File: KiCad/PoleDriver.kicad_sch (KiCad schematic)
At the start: 6 parts, among them Q301 AGM6014AP, Q303 AGM6014AP

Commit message: start adding control pins
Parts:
- R301, R302: footprint (none) -> Resistor_SMD:R_0402_1005Metric
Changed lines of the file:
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@@
 					(unit 1)
 				)
-				(path "/0dffc378-5905-459a-b0cb-e8e514a8bbef/e842f42e-62e8-4809-9799-e9078ef99b24/20b87812-a82e-42f6-920a-0aca573365c0"
-					(reference "C801")
-					(unit 1)
-				)
-				(path "/0dffc378-5905-459a-b0cb-e8e514a8bbef/e842f42e-62e8-4809-9799-e9078ef99b24/cd26c950-3a70-43f9-bc93-52ca2ff7311f"
-					(reference "C901")
-					(unit 1)
-				)
-				(path "/0dffc378-5905-459a-b0cb-e8e514a8bbef/e842f42e-62e8-4809-9799-e9078ef99b24/ee00243c-0671-4d24-ad12-35a8d122e435"
-					(reference "C701")
+				(path "/0dffc378-5905-459a-b0cb-e8e514a8bbef/f2c2b770-272c-4740-ba73-c3bb2a232079/20b87812-a82e-42f6-920a-0aca573365c0"
+					(reference "C110")
+					(unit 1)
+				)
+				(path "/0dffc378-5905-459a-b0cb-e8e514a8bbef/f2c2b770-272c-4740-ba73-c3bb2a232079/cd26c950-3a70-43f9-bc93-52ca2ff7311f"
+					(reference "C108")
+					(unit 1)
+				)
+				(path "/0dffc378-5905-459a-b0cb-e8e514a8bbef/f2c2b770-272c-4740-ba73-c3bb2a232079/ee00243c-0671-4d24-ad12-35a8d122e435"
+					(reference "C109")
 					(unit 1)
 				)
@@
 					(unit 1)
 				)
-				(path "/0dffc378-5905-459a-b0cb-e8e514a8bbef/e842f42e-62e8-4809-9799-e9078ef99b24/20b87812-a82e-42f6-920a-0aca573365c0"
-					(reference "#PWR0801")
-					(unit 1)
-				)
-				(path "/0dffc378-5905-459a-b0cb-e8e514a8bbef/e842f42e-62e8-4809-9799-e9078ef99b24/cd26c950-3a70-43f9-bc93-52ca2ff7311f"
-					(reference "#PWR0901")
-					(unit 1)
-				)
-				(path "/0dffc378-5905-459a-b0cb-e8e514a8bbef/e842f42e-62e8-4809-9799-e9078ef99b24/ee00243c-0671-4d24-ad12-35a8d122e435"
-					(reference "#PWR0701")
+				(path "/0dffc378-5905-459a-b0cb-e8e514a8bbef/f2c2b770-272c-4740-ba73-c3bb2a232079/20b87812-a82e-42f6-920a-0aca573365c0"
+					(reference "#PWR0112")
+					(unit 1)
+				)
+				(path "/0dffc378-5905-459a-b0cb-e8e514a8bbef/f2c2b770-272c-4740-ba73-c3bb2a232079/cd26c950-3a70-43f9-bc93-52ca2ff7311f"
+					(reference "#PWR0110")
+					(unit 1)
+				)
+				(path "/0dffc378-5905-459a-b0cb-e8e514a8bbef/f2c2b770-272c-4740-ba73-c3bb2a232079/ee00243c-0671-4d24-ad12-35a8d122e435"
+					(reference "#PWR0111")
 					(unit 1)
 				)
@@
 			)
 		)
-		(property "Footprint" ""
+		(property "Footprint" "Resistor_SMD:R_0402_1005Metric"
 			(at 83.82 36.83 0)
 			(hide yes)
@@
 					(unit 1)
 				)
-				(path "/0dffc378-5905-459a-b0cb-e8e514a8bbef/e842f42e-62e8-4809-9799-e9078ef99b24/20b87812-a82e-42f6-920a-0aca573365c0"
-					(reference "R802")
-					(unit 1)
-				)
-				(path "/0dffc378-5905-459a-b0cb-e8e514a8bbef/e842f42e-62e8-4809-9799-e9078ef99b24/cd26c950-3a70-43f9-bc93-52ca2ff7311f"
-					(reference "R902")
-					(unit 1)
-				)
-				(path "/0dffc378-5905-459a-b0cb-e8e514a8bbef/e842f42e-62e8-4809-9799-e9078ef99b24/ee00243c-0671-4d24-ad12-35a8d122e435"
-					(reference "R702")
+				(path "/0dffc378-5905-459a-b0cb-e8e514a8bbef/f2c2b770-272c-4740-ba73-c3bb2a232079/20b87812-a82e-42f6-920a-0aca573365c0"
+					(reference "R103")
+					(unit 1)
+				)
+				(path "/0dffc378-5905-459a-b0cb-e8e514a8bbef/f2c2b770-272c-4740-ba73-c3bb2a232079/cd26c950-3a70-43f9-bc93-52ca2ff7311f"
+					(reference "R101")
+					(unit 1)
+				)
+				(path "/0dffc378-5905-459a-b0cb-e8e514a8bbef/f2c2b770-272c-4740-ba73-c3bb2a232079/ee00243c-0671-4d24-ad12-35a8d122e435"
+					(reference "R102")
 					(unit 1)
 				)
@@
 					(unit 1)
 				)
-				(path "/0dffc378-5905-459a-b0cb-e8e514a8bbef/e842f42e-62e8-4809-9799-e9078ef99b24/20b87812-a82e-42f6-920a-0aca573365c0"
-					(reference "Q801")
-					(unit 1)
-				)
-				(path "/0dffc378-5905-459a-b0cb-e8e514a8bbef/e842f42e-62e8-4809-9799-e9078ef99b24/cd26c950-3a70-43f9-bc93-52ca2ff7311f"
-					(reference "Q901")
-					(unit 1)
-				)
-				(path "/0dffc378-5905-459a-b0cb-e8e514a8bbef/e842f42e-62e8-4809-9799-e9078ef99b24/ee00243c-0671-4d24-ad12-35a8d122e435"
-					(reference "Q701")
+				(path "/0dffc378-5905-459a-b0cb-e8e514a8bbef/f2c2b770-272c-4740-ba73-c3bb2a232079/20b87812-a82e-42f6-920a-0aca573365c0"
+					(reference "Q103")
+					(unit 1)
+				)
+				(path "/0dffc378-5905-459a-b0cb-e8e514a8bbef/f2c2b770-272c-4740-ba73-c3bb2a232079/cd26c950-3a70-43f9-bc93-52ca2ff7311f"
+					(reference "Q101")
+					(unit 1)
+				)
+				(path "/0dffc378-5905-459a-b0cb-e8e514a8bbef/f2c2b770-272c-4740-ba73-c3bb2a232079/ee00243c-0671-4d24-ad12-35a8d122e435"
+					(reference "Q102")
 					(unit 1)
 				)
@@
 					(unit 1)
 				)
-				(path "/0dffc378-5905-459a-b0cb-e8e514a8bbef/e842f42e-62e8-4809-9799-e9078ef99b24/20b87812-a82e-42f6-920a-0aca573365c0"
-					(reference "Q803")
-					(unit 1)
-				)
-				(path "/0dffc378-5905-459a-b0cb-e8e514a8bbef/e842f42e-62e8-4809-9799-e9078ef99b24/cd26c950-3a70-43f9-bc93-52ca2ff7311f"
-					(reference "Q903")
-					(unit 1)
-				)
-				(path "/0dffc378-5905-459a-b0cb-e8e514a8bbef/e842f42e-62e8-4809-9799-e9078ef99b24/ee00243c-0671-4d24-ad12-35a8d122e435"
-					(reference "Q703")
+				(path "/0dffc378-5905-459a-b0cb-e8e514a8bbef/f2c2b770-272c-4740-ba73-c3bb2a232079/20b87812-a82e-42f6-920a-0aca573365c0"
+					(reference "Q106")
+					(unit 1)
+				)
+				(path "/0dffc378-5905-459a-b0cb-e8e514a8bbef/f2c2b770-272c-4740-ba73-c3bb2a232079/cd26c950-3a70-43f9-bc93-52ca2ff7311f"
+					(reference "Q104")
+					(unit 1)
+				)
+				(path "/0dffc378-5905-459a-b0cb-e8e514a8bbef/f2c2b770-272c-4740-ba73-c3bb2a232079/ee00243c-0671-4d24-ad12-35a8d122e435"
+					(reference "Q105")
 					(unit 1)
 				)
@@
 			)
 		)
-		(property "Footprint" ""
+		(property "Footprint" "Resistor_SMD:R_0402_1005Metric"
 			(at 83.82 59.69 0)
 			(hide yes)
@@
 					(unit 1)
 				)
-				(path "/0dffc378-5905-459a-b0cb-e8e514a8bbef/e842f42e-62e8-4809-9799-e9078ef99b24/20b87812-a82e-42f6-920a-0aca573365c0"
-					(reference "R801")
-					(unit 1)
-				)
-				(path "/0dffc378-5905-459a-b0cb-e8e514a8bbef/e842f42e-62e8-4809-9799-e9078ef99b24/cd26c950-3a70-43f9-bc93-52ca2ff7311f"
-					(reference "R901")
-					(unit 1)
-				)
-				(path "/0dffc378-5905-459a-b0cb-e8e514a8bbef/e842f42e-62e8-4809-9799-e9078ef99b24/ee00243c-0671-4d24-ad12-35a8d122e435"
-					(reference "R701")
+				(path "/0dffc378-5905-459a-b0cb-e8e514a8bbef/f2c2b770-272c-4740-ba73-c3bb2a232079/20b87812-a82e-42f6-920a-0aca573365c0"
+					(reference "R106")
+					(unit 1)
+				)
+				(path "/0dffc378-5905-459a-b0cb-e8e514a8bbef/f2c2b770-272c-4740-ba73-c3bb2a232079/cd26c950-3a70-43f9-bc93-52ca2ff7311f"
+					(reference "R104")
+					(unit 1)
+				)
+				(path "/0dffc378-5905-459a-b0cb-e8e514a8bbef/f2c2b770-272c-4740-ba73-c3bb2a232079/ee00243c-0671-4d24-ad12-35a8d122e435"
+					(reference "R105")
 					(unit 1)
 				)
@@
 					(unit 1)
 				)
-				(path "/0dffc378-5905-459a-b0cb-e8e514a8bbef/e842f42e-62e8-4809-9799-e9078ef99b24/20b87812-a82e-42f6-920a-0aca573365c0"
-					(reference "Rsns801")
-					(unit 1)
-				)
-				(path "/0dffc378-5905-459a-b0cb-e8e514a8bbef/e842f42e-62e8-4809-9799-e9078ef99b24/cd26c950-3a70-43f9-bc93-52ca2ff7311f"
-					(reference "Rsns901")
-					(unit 1)
-				)
-				(path "/0dffc378-5905-459a-b0cb-e8e514a8bbef/e842f42e-62e8-4809-9799-e9078ef99b24/ee00243c-0671-4d24-ad12-35a8d122e435"
-					(reference "Rsns701")
-					(unit 1)
-				)
+				(path "/0dffc378-5905-459a-b0cb-e8e514a8bbef/f2c2b770-272c-4740-ba73-c3bb2a232079/20b87812-a82e-42f6-920a-0aca573365c0"
+					(reference "Rsns103")
+					(unit 1)
+				)
+				(path "/0dffc378-5905-459a-b0cb-e8e514a8bbef/f2c2b770-272c-4740-ba73-c3bb2a232079/cd26c950-3a70-43f9-bc93-52ca2ff7311f"
+					(reference "Rsns101")
+					(unit 1)
+				)
+				(path "/0dffc378-5905-459a-b0cb-e8e514a8bbef/f2c2b770-272c-4740-ba73-c3bb2a232079/ee00243c-0671-4d24-ad12-35a8d122e435"
+					(reference "Rsns102")
+					(unit 1)
+				)

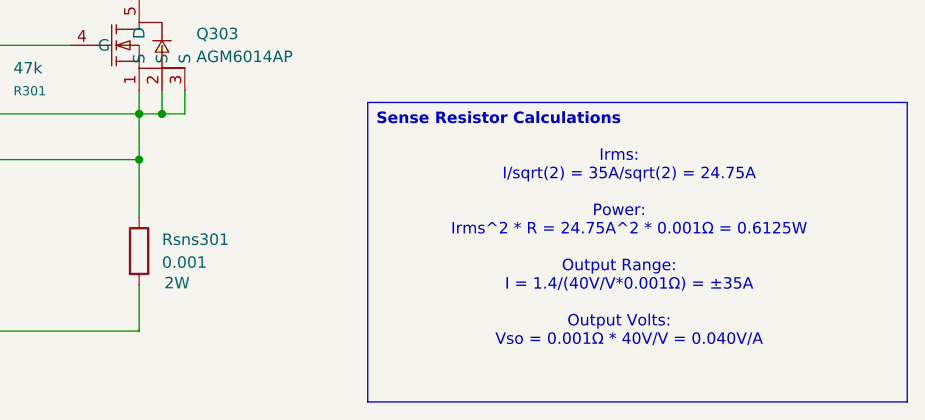
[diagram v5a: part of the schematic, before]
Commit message: updated configuration for new mosfets
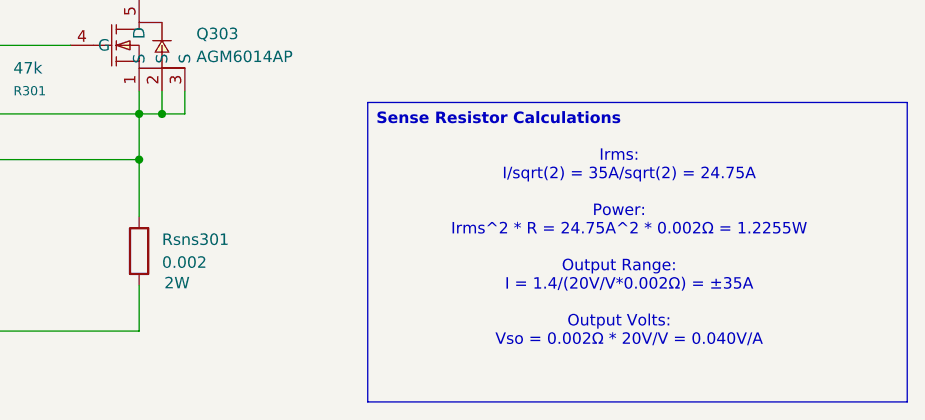
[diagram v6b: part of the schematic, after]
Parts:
- Rsns301: value 0.001 -> 0.002
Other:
- note added: "Irms: I/sqrt(2) = 35A/sqrt(2) = 24.75A Power: Irms^2 * R = 24.75A^2 * 0.002Ω = 1.2255W Output Range: I = 1.4/(20V/V*0.002Ω) = ±35A Output Volts: Vso = 0.002Ω * 20V/V = 0.040V/A"
- note removed: "Irms: I/sqrt(2) = 35A/sqrt(2) = 24.75A Power: Irms^2 * R = 24.75A^2 * 0.001Ω = 0.6125W Output Range: I = 1.4/(40V/V*0.001Ω) = ±35A Output Volts: Vso = 0.001Ω * 40V/V = 0.040V/A"
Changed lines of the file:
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@@
 		(title "Motor Pole Half-Bridge")
 	)
-	(text "Irms:\n	I/sqrt(2) = 35A/sqrt(2) = 24.75A\n\nPower:\n	Irms^2 * R = 24.75A^2 * 0.001Ω = 0.6125W\n\nOutput Range:\n	I = 1.4/(40V/V*0.001Ω) = ±35A\n\nOutput Volts:\n	Vso = 0.001Ω * 40V/V = 0.040V/A"
+	(text "Irms:\n	I/sqrt(2) = 35A/sqrt(2) = 24.75A\n\nPower:\n	Irms^2 * R = 24.75A^2 * 0.002Ω = 1.2255W\n\nOutput Range:\n	I = 1.4/(20V/V*0.002Ω) = ±35A\n\nOutput Volts:\n	Vso = 0.002Ω * 20V/V = 0.040V/A"
 		(exclude_from_sim no)
 		(at 153.67 78.486 0)
@@
 			)
 		)
-		(property "Value" "0.001"
+		(property "Value" "0.002"
 			(at 102.87 80.0099 0)
 			(show_name no)

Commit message: finished iteration 1
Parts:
- removed Q301, Q303: AGM6014AP, easyeda2kicad:PDFN-8_L3.1-W3.0-P0.65-LS3.3-BL, symbol easyeda2kicad:AGM6014AP
- added Q301, Q302: XRS100N06LD, easyeda2kicad:DFN-8_L3.0-W3.0-P0.65-BL-4, symbol easyeda2kicad:XRS100N06LD
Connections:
- net GH: now also Q302.4 (G)
- net GL: now also Q301.4 (G)
- net PoleOut: now also Q301.5 (D), Q302.1 (S), Q302.2 (S), Q302.3 (S)
- net SP: now also Q301.1 (S), Q301.2 (S), Q301.3 (S)
- net V+: now also Q302.5 (D)
